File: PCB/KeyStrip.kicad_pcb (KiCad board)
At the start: 2 copper layers, 3.4 x 4 mm, 19 parts, among them J2 JST_08

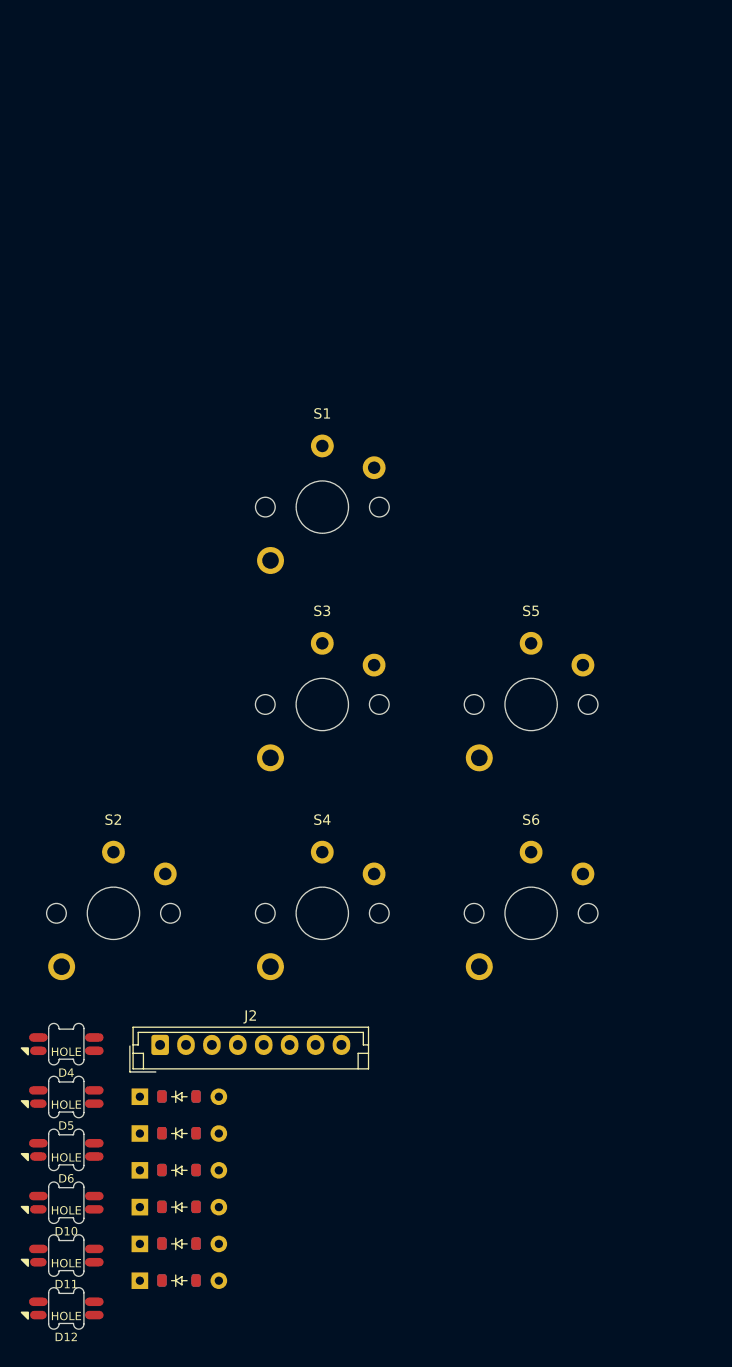
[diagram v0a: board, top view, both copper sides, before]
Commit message: Actually well routed and placed this time
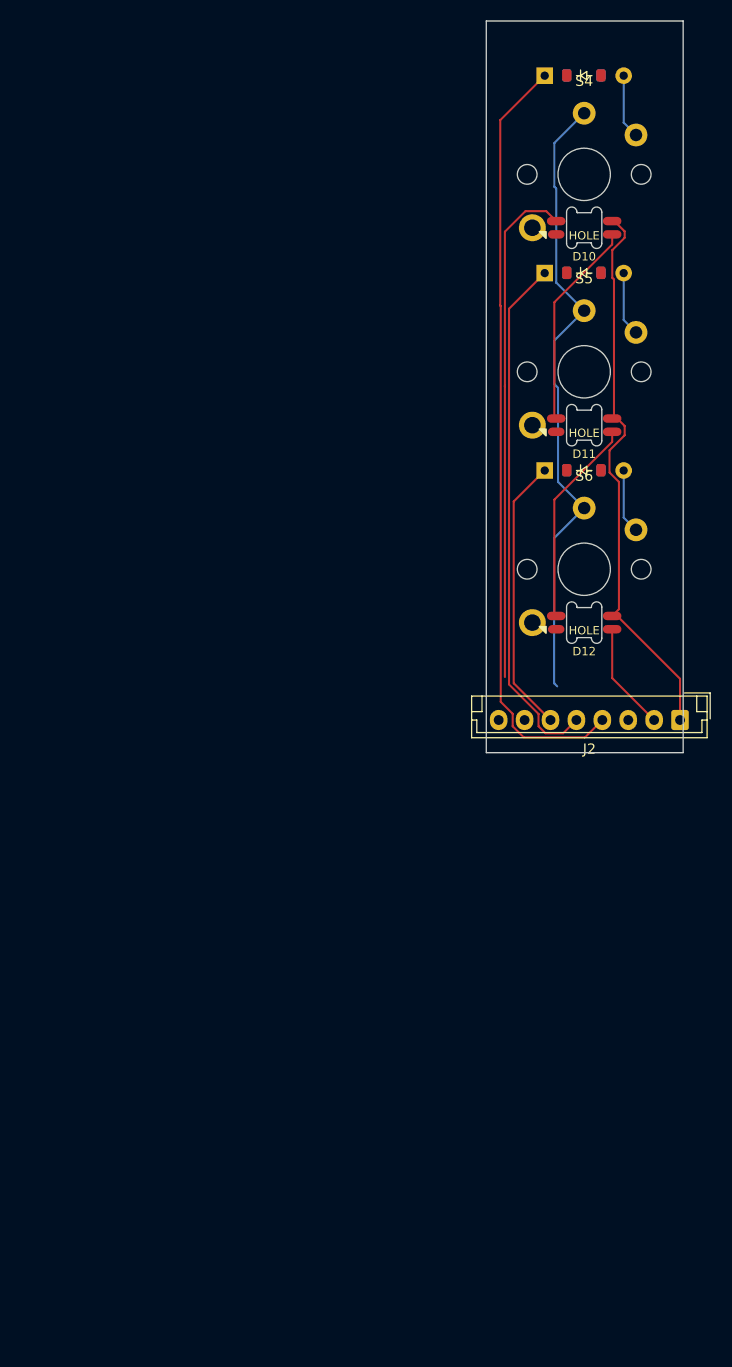
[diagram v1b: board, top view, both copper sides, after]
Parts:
- removed D1, D2, D3: Diode, Library:DualDiode
- removed D4, D5, D6: LED_SK6812MINI, Library:SK6812Mini-E
- removed S1, S2, S3: Keyswitch, Library:Choc_V1V2_1.00u
- moved D7 116.0 mm to (67.4, 59.6)
- moved D10 106.5 mm to (71.2, 74.3)
- moved D8 101.5 mm to (67.4, 78.7)
- moved D11 94.4 mm to (71.2, 93.3)
- moved D9 87.4 mm to (67.4, 97.7)
- moved D12 82.9 mm to (71.2, 112.4)
- moved S4 75.6 mm to (71.2, 69.2)
- moved J2 59.2 mm to (80.5, 121.8), turned to 180 degrees
- moved S6 33.6 mm to (71.2, 107.2)
- moved S5 32.5 mm to (71.2, 88.2)
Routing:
- net Net-(D7-K): track 0.00 -> 74.8 mm
- net Net-(J2-Pad7): track 0.00 -> 61.4 mm
- net Net-(D10-VDD): track 0.00 -> 54.4 mm
- net Net-(D8-K): track 0.00 -> 50.8 mm
- net Net-(D10-DIN): track 0.00 -> 49.2 mm
- net Net-(D9-K): track 0.00 -> 26.8 mm
- net Net-(D11-DOUT): track 0.00 -> 20.2 mm
- net Net-(D10-DOUT): track 0.00 -> 20.2 mm
- net Net-(D12-DOUT): track 0.00 -> 10.4 mm
- net Net-(D9-A): track 0.00 -> 6.22 mm
- net Net-(D8-A): track 0.00 -> 6.22 mm
- net Net-(D7-A): track 0.00 -> 6.22 mm
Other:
- board size 3.4 x 4 mm -> 19 x 70.6 mm

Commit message: I just gotta add screw holes and solo variations now
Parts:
- J2: footprint Connector_JST:JST_EH_B8B-EH-A_1x08_P2.50mm_Vertical -> Library:JST_EH_B8B-EH-A_1x08_P2.50mm_Vertical
- moved J2 4.78 mm to (78.0, 117.7)
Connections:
- J2 pad 1: Net-(D10-VDD) -> Net-(D10-VSS)
- J2 pad 3: Net-(D10-DIN) -> Net-(D10-VDD)
- J2 pad 4: Net-(D7-K) -> Net-(J2-Pad4)
- J2 pad 5: Net-(D8-K) -> Net-(D9-K)
- J2 pad 6: Net-(D9-K) -> Net-(D8-K)
- J2 pad 7: Net-(J2-Pad7) -> Net-(D10-DIN)
- J2 pad 8: Net-(D10-VSS) -> Net-(D7-K)
- S4 pad 1: Net-(J2-Pad7) -> Net-(J2-Pad4)
- S5 pad 1: Net-(J2-Pad7) -> Net-(J2-Pad4)
- S6 pad 1: Net-(J2-Pad7) -> Net-(J2-Pad4)
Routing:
- net Net-(J2-Pad4): track 0.00 -> 61.9 mm
- net Net-(J2-Pad7): track 61.4 -> 0.00 mm
- net Net-(D7-K): track 74.8 -> 60.2 mm
- net Net-(D8-K): track 50.8 -> 42.1 mm
- net Net-(D12-DOUT): track 10.4 -> 5.53 mm
- net Net-(D10-VDD): track 54.4 -> 49.6 mm, vias 0 -> 1
- net Net-(D9-K): track 26.8 -> 24.7 mm
- net Net-(D10-DIN): track 49.2 -> 50.2 mm
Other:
- board size 19 x 70.6 mm -> 19.1 x 61 mm

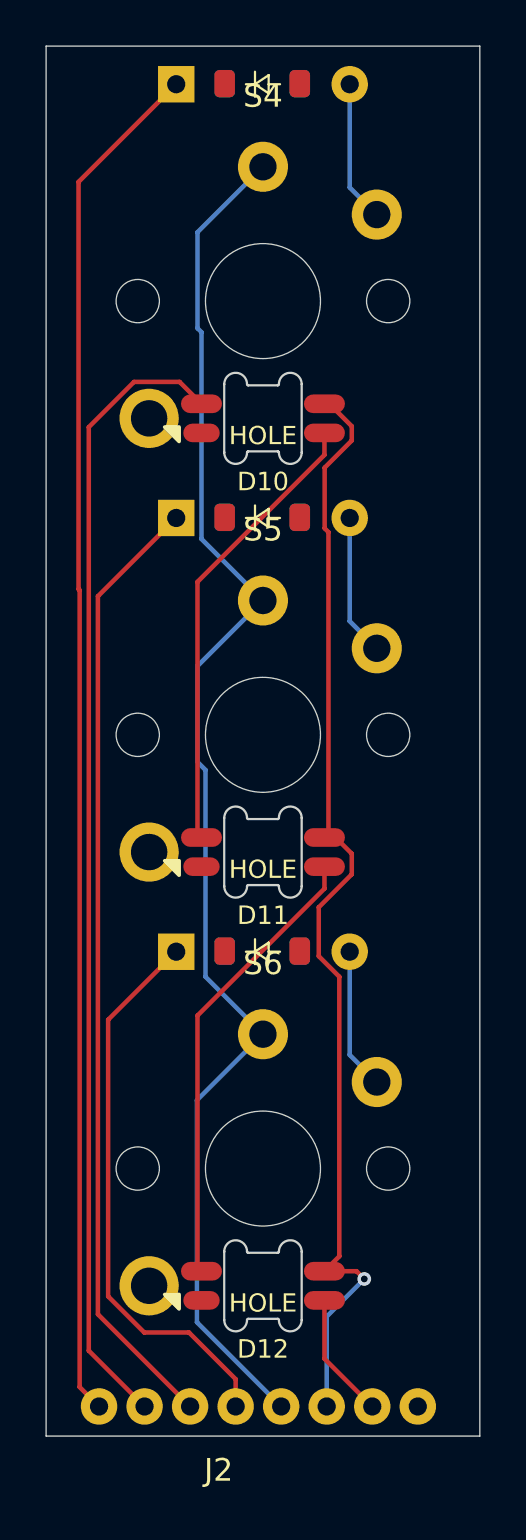
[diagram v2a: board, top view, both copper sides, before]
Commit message: Added screw holes and routed and fixed the thingy thing
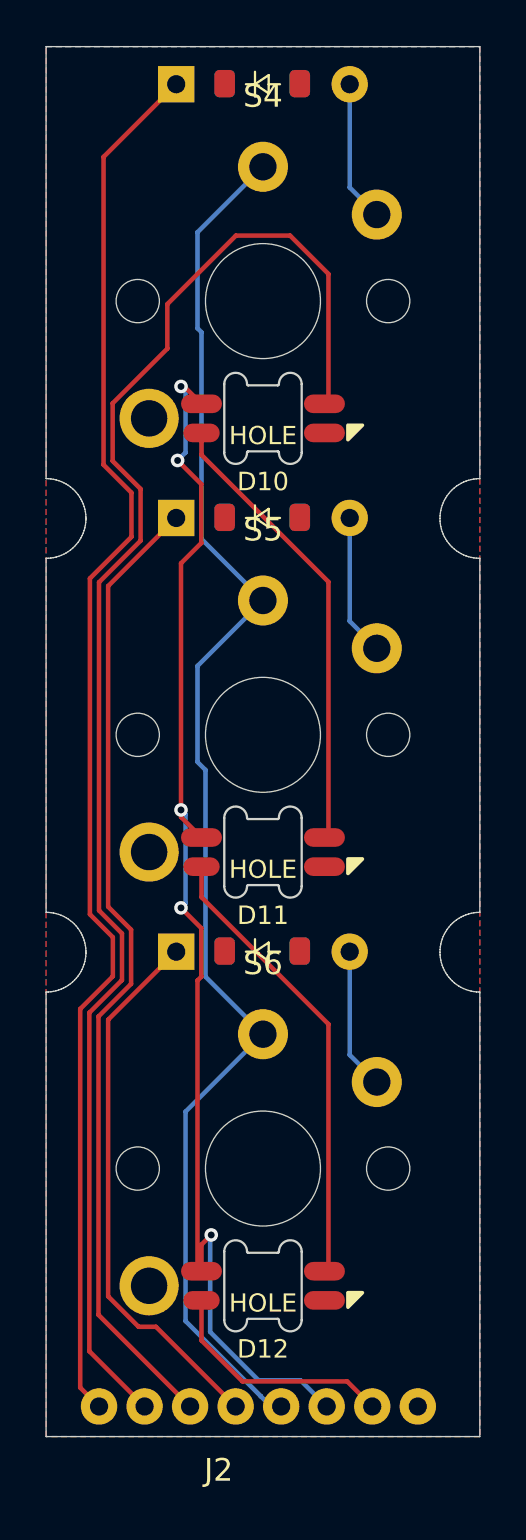
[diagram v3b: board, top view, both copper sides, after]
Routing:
- net Net-(D10-DIN): track 50.2 -> 67.5 mm
- net Net-(D10-VDD): track 49.6 -> 55.9 mm, vias 1 -> 5
- net Net-(D12-DOUT): track 5.53 -> 10.5 mm
- net Net-(D7-K): track 60.2 -> 62.0 mm
- net Net-(D8-K): track 42.1 -> 42.9 mm
- net Net-(D9-K): track 24.7 -> 24.0 mm
- net Net-(J2-Pad4): track 61.9 -> 62.6 mm
- added copper zone on B.Cu, net Net-(D10-VSS)
- added copper zone on F.Cu, net Net-(D10-VSS)
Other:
- outline, holes or cut-outs redrawn
